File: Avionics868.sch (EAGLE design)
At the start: 65 parts, among them SW1 SPST_TACT-KMR2, U1 ATSAMD21G18_QFN, U2 SPX3819M5-L-3-0, U3 MCP73831T-2ACI/OT, U4 MPU-9250, U5 SIM868, U6 BMP180, X1 JSTPH, X2 32.768, X3 microUSB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

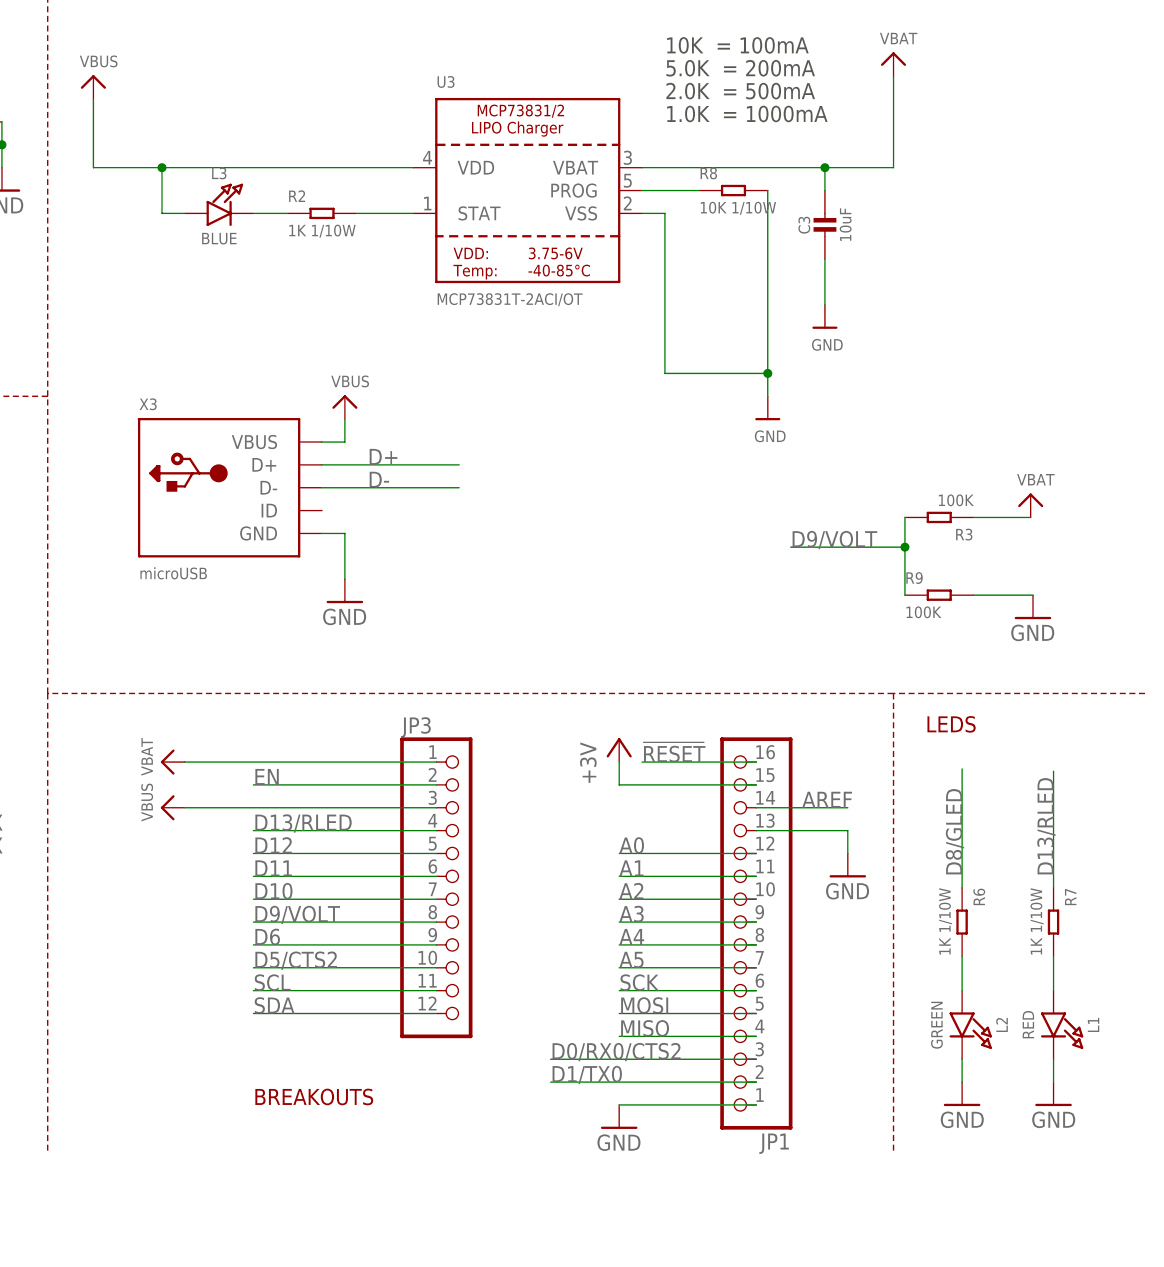
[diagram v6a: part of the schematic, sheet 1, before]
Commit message: Changed LEDs to Seeed ++
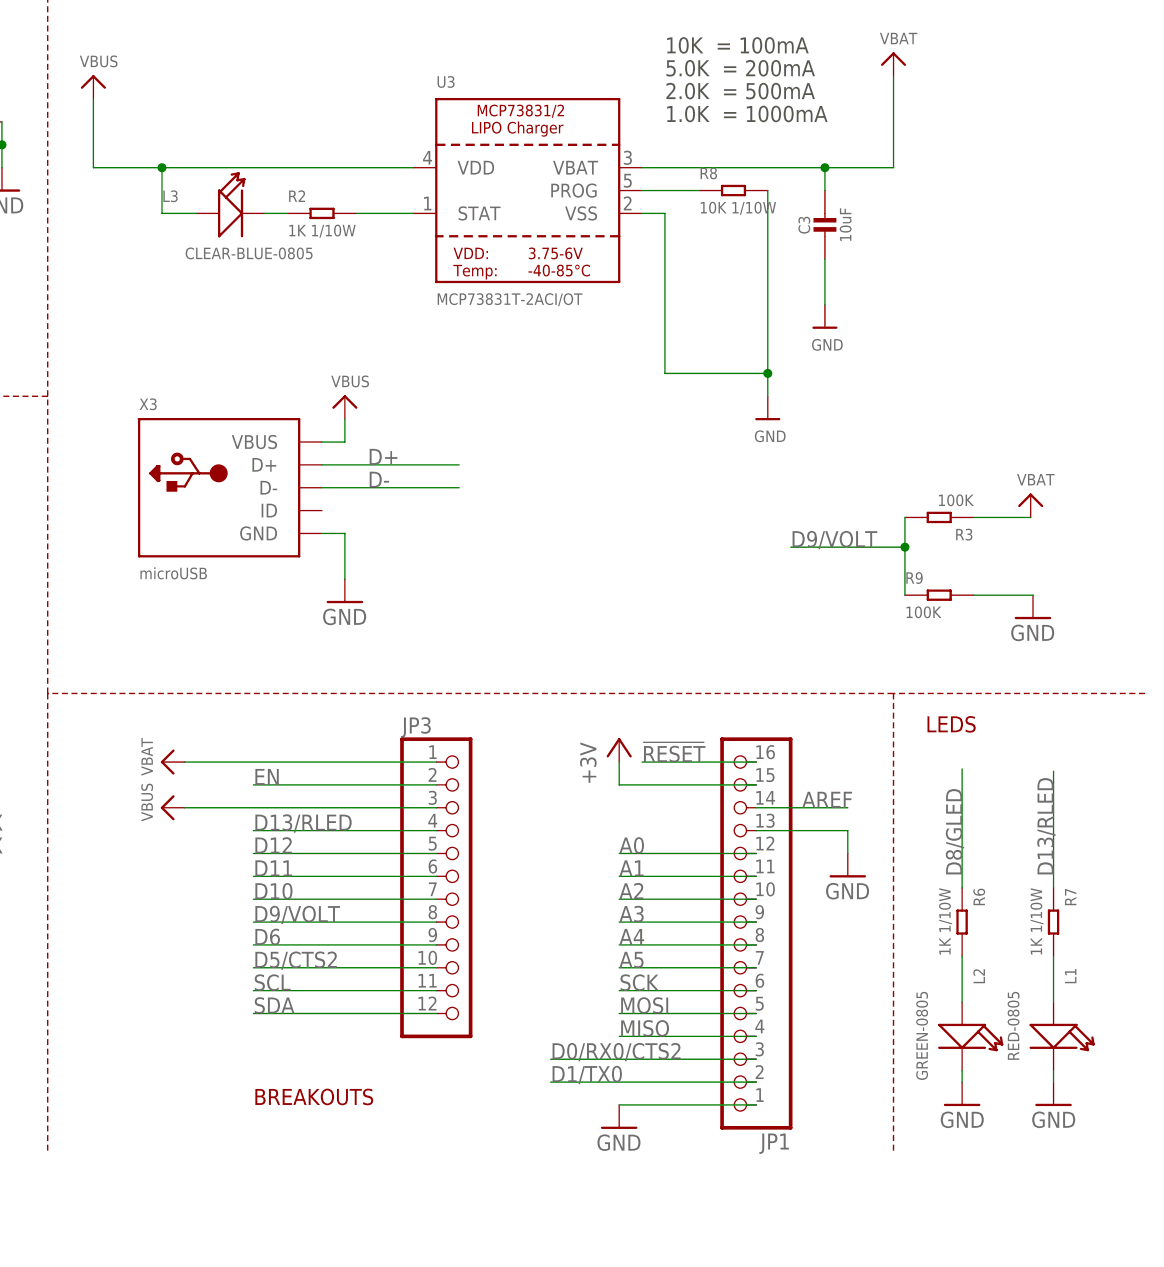
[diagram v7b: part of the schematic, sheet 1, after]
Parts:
- L1: value RED -> RED-0805; device microbuilder:LED0805_NOOUTLINE -> Seeed-LED-2016:SMD-LED-CLEAR-RED(0805)
- L2: value GREEN -> GREEN-0805; device microbuilder:LED0805_NOOUTLINE -> Seeed-LED-2016:SMD-LED-CLEAR-GREEN(0805)
- L3: value BLUE -> CLEAR-BLUE-0805; device microbuilder:LED0805_NOOUTLINE -> Seeed-LED-2016:SMD-LED-CLEAR-BLUE(0805)
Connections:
- net GND: now also L1.-, L2.-; no longer L1.C, L2.C
- net N$1: now also L3.-; no longer L3.C
- net N$2: now also L2.+, R6.2; no longer L1.A, R7.2
- net N$8: now also L1.+, R7.2; no longer L2.A, R6.2
- net VBUS: now also L3.+; no longer L3.A
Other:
- moved on the sheet: C21, C22
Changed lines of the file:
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@@
 <part name="GND1" library="supply1" deviceset="GND" device=""/>
 <part name="GND12" library="supply1" deviceset="GND" device=""/>
-<part name="L1" library="microbuilder" deviceset="LED" device="0805_NOOUTLINE" value="RED"/>
+<part name="L1" library="Seeed-LED-2016" deviceset="SMD-LED-CLEAR-RED(0805)" device="" value="RED-0805"/>
 <part name="GND7" library="supply1" deviceset="GND" device=""/>
 <part name="C14" library="microbuilder" deviceset="CAP_CERAMIC" device="0603_NO" value="1uF"/>
@@
 <part name="JP3" library="microbuilder" deviceset="HEADER-1X12" device=""/>
 <part name="U3" library="microbuilder" deviceset="MCP73831/2" device="" value="MCP73831T-2ACI/OT"/>
-<part name="L3" library="microbuilder" deviceset="LED" device="0805_NOOUTLINE" value="BLUE"/>
+<part name="L3" library="Seeed-LED-2016" deviceset="SMD-LED-CLEAR-BLUE(0805)" device="" value="CLEAR-BLUE-0805"/>
 <part name="R2" library="Seeed-Resistor-2016" deviceset="SMD-RES-1K-5%-1/10W(0603)" device="" value="1K 1/10W"/>
 <part name="C3" library="microbuilder" deviceset="CAP_CERAMIC" device="0805-NOOUTLINE" value="10uF"/>
@@
 <part name="JP2" library="SparkFun-Passives" deviceset="JUMPER-PAD-2-NC_BY_TRACE" device=""/>
 <part name="TP5" library="microbuilder" deviceset="TESTPOINT" device="ROUND1.5MM"/>
-<part name="L2" library="microbuilder" deviceset="LED" device="0805_NOOUTLINE" value="GREEN"/>
+<part name="L2" library="Seeed-LED-2016" deviceset="SMD-LED-CLEAR-GREEN(0805)" device="" value="GREEN-0805"/>
 <part name="R6" library="Seeed-Resistor-2016" deviceset="SMD-RES-1K-5%-1/10W(0603)" device="" value="1K 1/10W"/>
 <part name="GND9" library="supply1" deviceset="GND" device=""/>
@@
 <part name="+3V14" library="Custom" deviceset="+3V" device=""/>
 <part name="U$35" library="microbuilder" deviceset="GND" device=""/>
+<part name="U$51" library="microbuilder" deviceset="GND" device=""/>
 </parts>
 <sheets>
@@
 </segment>
 <segment>
-<pinref part="L1" gate="G$1" pin="C"/>
-<pinref part="GND10" gate="1" pin="GND"/>
-<wire x1="246.38" y1="48.26" x2="246.38" y2="45.72" width="0.1524" layer="91"/>
-</segment>
-<segment>
 <pinref part="JP1" gate="A" pin="13"/>
 <pinref part="GND4" gate="1" pin="GND"/>
@@
 </segment>
 <segment>
+<pinref part="GND10" gate="1" pin="GND"/>
+<pinref part="L1" gate="G$1" pin="-"/>
+<wire x1="246.38" y1="45.72" x2="246.38" y2="46.99" width="0.1524" layer="91"/>
+</segment>
+<segment>
+<pinref part="L2" gate="G$1" pin="-"/>
 <pinref part="GND9" gate="1" pin="GND"/>
-<pinref part="L2" gate="G$1" pin="C"/>
-<wire x1="236.22" y1="48.26" x2="236.22" y2="45.72" width="0.1524" layer="91"/>
+<wire x1="236.22" y1="46.99" x2="236.22" y2="45.72" width="0.1524" layer="91"/>
 </segment>
 </net>
@@
 <wire x1="139.7" y1="147.32" x2="147.32" y2="147.32" width="0.1524" layer="91"/>
 <wire x1="147.32" y1="147.32" x2="175.26" y2="147.32" width="0.1524" layer="91"/>
-<pinref part="L3" gate="G$1" pin="A"/>
-<wire x1="149.86" y1="142.24" x2="147.32" y2="142.24" width="0.1524" layer="91"/>
 <wire x1="147.32" y1="142.24" x2="147.32" y2="147.32" width="0.1524" layer="91"/>
 <junction x="147.32" y="147.32"/>
 <pinref part="U$38" gate="G$1" pin="VBUS"/>
+<pinref part="L3" gate="G$1" pin="+"/>
+<wire x1="151.13" y1="142.24" x2="147.32" y2="142.24" width="0.1524" layer="91"/>
 </segment>
 </net>
@@
 </segment>
 </net>
-<net name="N$2" class="0">
-<segment>
-<pinref part="L1" gate="G$1" pin="A"/>
-<pinref part="R7" gate="G$1" pin="2"/>
-<wire x1="246.38" y1="59.69" x2="246.38" y2="55.88" width="0.1524" layer="91"/>
-</segment>
-</net>
 <net name="D13/RLED" class="0">
 <segment>
@@
 <wire x1="104.14" y1="91.44" x2="121.92" y2="91.44" width="0.1524" layer="91"/>
 <label x="111.76" y="91.44" size="1.778" layer="95"/>
-</segment>
-</net>
-<net name="N$1" class="0">
-<segment>
-<pinref part="L3" gate="G$1" pin="C"/>
-<pinref part="R2" gate="G$1" pin="1"/>
-<wire x1="157.48" y1="142.24" x2="161.29" y2="142.24" width="0.1524" layer="91"/>
 </segment>
 </net>
@@
 </segment>
 </net>
+<net name="N$1" class="0">
+<segment>
+<pinref part="L3" gate="G$1" pin="-"/>
+<pinref part="R2" gate="G$1" pin="1"/>
+<wire x1="158.75" y1="142.24" x2="161.29" y2="142.24" width="0.1524" layer="91"/>
+</segment>
+</net>
+<net name="N$2" class="0">
+<segment>
+<pinref part="R6" gate="G$1" pin="2"/>
+<pinref part="L2" gate="G$1" pin="+"/>
+<wire x1="236.22" y1="59.69" x2="236.22" y2="54.61" width="0.1524" layer="91"/>
+</segment>
+</net>
 <net name="N$8" class="0">
 <segment>
-<pinref part="L2" gate="G$1" pin="A"/>
-<pinref part="R6" gate="G$1" pin="2"/>
-<wire x1="236.22" y1="59.69" x2="236.22" y2="55.88" width="0.1524" layer="91"/>
+<pinref part="R7" gate="G$1" pin="2"/>
+<pinref part="L1" gate="G$1" pin="+"/>
+<wire x1="246.38" y1="59.69" x2="246.38" y2="54.61" width="0.1524" layer="91"/>
 </segment>
 </net>
@@
 <instance part="+3V5" gate="G$1" x="15.24" y="78.74" rot="MR0"/>
 <instance part="U$45" gate="G$1" x="15.24" y="53.34"/>
-<instance part="C21" gate="G$1" x="48.514" y="113.538" rot="R270"/>
-<instance part="U$49" gate="G$1" x="48.514" y="101.092"/>
-<instance part="C22" gate="G$1" x="58.42" y="113.538" rot="R90"/>
-<instance part="U$50" gate="G$1" x="58.42" y="101.092"/>
+<instance part="C21" gate="G$1" x="47.752" y="110.49" rot="R270"/>
+<instance part="U$49" gate="G$1" x="47.752" y="104.14"/>
+<instance part="C22" gate="G$1" x="57.658" y="110.49" rot="R90"/>
+<instance part="U$50" gate="G$1" x="57.658" y="104.14"/>
 <instance part="C23" gate="G$1" x="71.374" y="121.158" rot="R270"/>
 <instance part="C24" gate="G$1" x="81.28" y="121.158" rot="R90"/>
-<instance part="+3V14" gate="G$1" x="76.708" y="127.508" smashed="yes" rot="MR0">
-<attribute name="VALUE" x="75.184" y="125.73" size="1.27" layer="96" rot="MR0"/>
-</instance>
-<instance part="U$35" gate="G$1" x="76.454" y="114.808"/>
+<instance part="+3V14" gate="G$1" x="76.2" y="130.556" smashed="yes" rot="MR0">
+<attribute name="VALUE" x="74.676" y="128.778" size="1.27" layer="96" rot="MR0"/>
+</instance>
+<instance part="U$35" gate="G$1" x="71.374" y="114.808"/>
+<instance part="U$51" gate="G$1" x="81.28" y="114.808"/>
 </instances>
 <busses>
@@
 <pinref part="C21" gate="G$1" pin="2"/>
 <pinref part="U$49" gate="G$1" pin="GND"/>
-<wire x1="48.514" y1="103.632" x2="48.514" y2="109.728" width="0.1524" layer="91"/>
 </segment>
 <segment>
 <pinref part="C22" gate="G$1" pin="1"/>
 <pinref part="U$50" gate="G$1" pin="GND"/>
-<wire x1="58.42" y1="103.632" x2="58.42" y2="109.728" width="0.1524" layer="91"/>
+</segment>
+<segment>
+<pinref part="C23" gate="G$1" pin="2"/>
+<pinref part="U$35" gate="G$1" pin="GND"/>
 </segment>
 <segment>
 <pinref part="C24" gate="G$1" pin="1"/>
-<pinref part="C23" gate="G$1" pin="2"/>
-<wire x1="81.28" y1="117.348" x2="76.454" y2="117.348" width="0.1524" layer="91"/>
-<pinref part="U$35" gate="G$1" pin="GND"/>
-<wire x1="76.454" y1="117.348" x2="71.374" y2="117.348" width="0.1524" layer="91"/>
-<junction x="76.454" y="117.348"/>
+<pinref part="U$51" gate="G$1" pin="GND"/>
 </segment>
 </net>
@@
 <pinref part="C23" gate="G$1" pin="1"/>
 <pinref part="C24" gate="G$1" pin="2"/>
-<wire x1="71.374" y1="124.968" x2="76.708" y2="124.968" width="0.1524" layer="91"/>
+<wire x1="71.374" y1="124.968" x2="76.2" y2="124.968" width="0.1524" layer="91"/>
 <pinref part="+3V14" gate="G$1" pin="+3V"/>
-<wire x1="76.708" y1="124.968" x2="81.28" y2="124.968" width="0.1524" layer="91"/>
-<junction x="76.708" y="124.968"/>
+<wire x1="76.2" y1="124.968" x2="81.28" y2="124.968" width="0.1524" layer="91"/>
+<wire x1="76.2" y1="128.016" x2="76.2" y2="124.968" width="0.1524" layer="91"/>
+<junction x="76.2" y="124.968"/>
 </segment>
 </net>
@@
 </segment>
 <segment>
+<pinref part="C21" gate="G$1" pin="1"/>
+<wire x1="52.578" y1="114.3" x2="52.578" y2="120.396" width="0.1524" layer="91"/>
+<wire x1="52.578" y1="114.3" x2="47.752" y2="114.3" width="0.1524" layer="91"/>
+<wire x1="52.578" y1="114.3" x2="57.658" y2="114.3" width="0.1524" layer="91"/>
 <pinref part="C22" gate="G$1" pin="2"/>
-<wire x1="58.42" y1="117.348" x2="58.42" y2="121.92" width="0.1524" layer="91"/>
-<label x="58.42" y="121.92" size="1.778" layer="95" rot="R90"/>
-<pinref part="C21" gate="G$1" pin="1"/>
-<wire x1="58.42" y1="121.92" x2="58.42" y2="125.476" width="0.1524" layer="91"/>
-<wire x1="48.514" y1="117.348" x2="48.514" y2="121.92" width="0.1524" layer="91"/>
-<wire x1="58.42" y1="121.92" x2="48.514" y2="121.92" width="0.1524" layer="91"/>
-</segment>
-</net>
+<junction x="52.578" y="114.3"/>
+<label x="52.07" y="115.57" size="1.778" layer="95" rot="R90"/>
+</segment>
+</net>

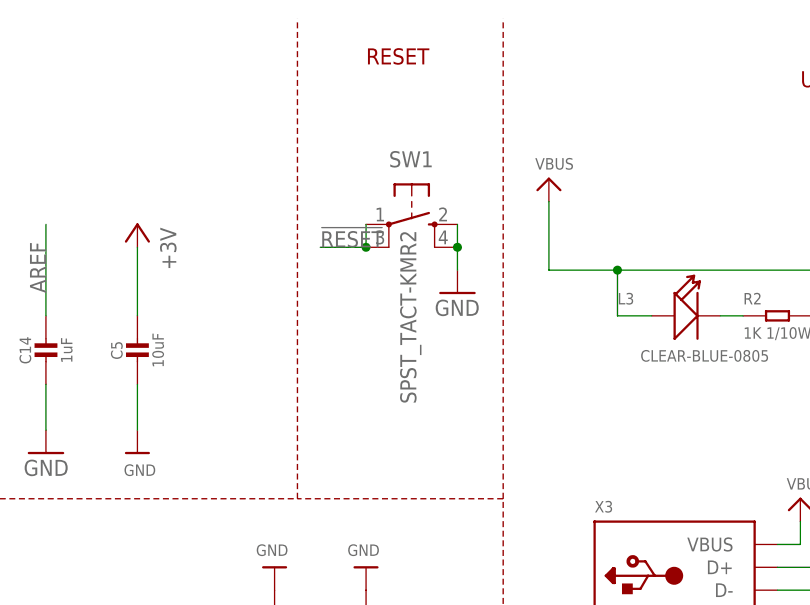
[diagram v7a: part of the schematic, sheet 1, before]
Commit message: Swapped switch for Seeed version
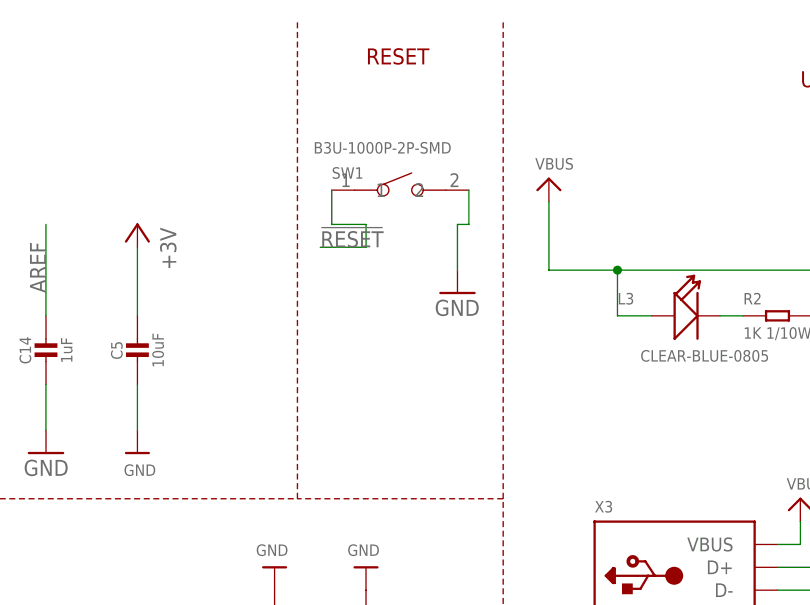
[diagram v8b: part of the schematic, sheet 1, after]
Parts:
- SW1: value SPST_TACT-KMR2 -> B3U-1000P-2P-SMD; device adafruit:SPST_TACT-KMR2 -> Seeed-Switch-2016:SMD-BUTTON(2P-3.0X2.5X1.2+0.4MM)-B3U-1000P-2P-SMD
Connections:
- net !RESET: now also SW1.1; no longer SW1.P, SW1.P1
- net GND: now also SW1.2; no longer SW1.S, SW1.S1
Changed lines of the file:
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@@
 <part name="GND10" library="supply1" deviceset="GND" device=""/>
 <part name="U$34" library="microbuilder" deviceset="FIDUCIAL" device="&quot;&quot;"/>
-<part name="SW1" library="adafruit" deviceset="SPST_TACT" device="-KMR2"/>
 <part name="U$31" library="microbuilder" deviceset="MOUNTINGHOLE" device="2.5"/>
 <part name="U$32" library="microbuilder" deviceset="MOUNTINGHOLE" device="2.5"/>
@@
 <part name="U$35" library="microbuilder" deviceset="GND" device=""/>
 <part name="U$51" library="microbuilder" deviceset="GND" device=""/>
+<part name="SW1" library="Seeed-Switch-2016" deviceset="SMD-BUTTON(2P-3.0X2.5X1.2+0.4MM)" device="-B3U-1000P-2P-SMD" value="B3U-1000P-2P-SMD"/>
 </parts>
 <sheets>
@@
 <instance part="GND10" gate="1" x="246.38" y="43.18" rot="MR0"/>
 <instance part="U$34" gate="G$1" x="210.82" y="17.78"/>
-<instance part="SW1" gate="G$1" x="124.46" y="152.4" smashed="yes" rot="R270">
-<attribute name="NAME" x="121.92" y="158.75" size="1.778" layer="95"/>
-<attribute name="VALUE" x="123.19" y="151.765" size="1.778" layer="96" rot="R270"/>
-</instance>
 <instance part="U$31" gate="G$1" x="205.74" y="12.7"/>
 <instance part="U$32" gate="G$1" x="210.82" y="12.7"/>
@@
 <instance part="U$2" gate="G$1" x="243.84" y="110.998"/>
 <instance part="GND13" gate="1" x="244.094" y="97.282"/>
+<instance part="SW1" gate="G$1" x="123.19" y="156.21" smashed="yes">
+<attribute name="NAME" x="115.57" y="157.48" size="1.27" layer="95" ratio="10"/>
+<attribute name="VALUE" x="113.538" y="160.274" size="1.27" layer="96" ratio="10"/>
+</instance>
 </instances>
 <busses>
@@
 </segment>
 <segment>
-<wire x1="129.54" y1="147.32" x2="129.54" y2="149.86" width="0.1524" layer="91"/>
-<wire x1="129.54" y1="152.4" x2="129.54" y2="149.86" width="0.1524" layer="91"/>
-<junction x="129.54" y="149.86"/>
+<wire x1="129.54" y1="152.4" x2="129.54" y2="147.32" width="0.1524" layer="91"/>
 <pinref part="GND7" gate="1" pin="GND"/>
-<pinref part="SW1" gate="G$1" pin="S"/>
-<pinref part="SW1" gate="G$1" pin="S1"/>
+<pinref part="SW1" gate="G$1" pin="2"/>
+<wire x1="129.54" y1="152.4" x2="130.81" y2="152.4" width="0.1524" layer="91"/>
+<wire x1="130.81" y1="152.4" x2="130.81" y2="156.21" width="0.1524" layer="91"/>
 </segment>
 <segment>
@@
 <wire x1="119.38" y1="149.86" x2="119.38" y2="152.4" width="0.1524" layer="91"/>
 <wire x1="114.3" y1="149.86" x2="119.38" y2="149.86" width="0.1524" layer="91"/>
-<junction x="119.38" y="149.86"/>
 <label x="114.3" y="149.86" size="1.778" layer="95"/>
-<pinref part="SW1" gate="G$1" pin="P"/>
-<pinref part="SW1" gate="G$1" pin="P1"/>
-</segment>
-<segment>
+<pinref part="SW1" gate="G$1" pin="1"/>
+<wire x1="119.38" y1="152.4" x2="115.57" y2="152.4" width="0.1524" layer="91"/>
+<wire x1="115.57" y1="152.4" x2="115.57" y2="156.21" width="0.1524" layer="91"/>
+</segment>
+<segment>
